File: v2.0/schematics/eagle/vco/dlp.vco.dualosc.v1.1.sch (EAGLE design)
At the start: 58 parts, among them IC1 NTE912P, IC2 TL074P, IC3 TL074P, J1 PWM IN1, J4 EXP.IN1, J6 OSC OUT1, Q1 2N3417, Q2 2N3417, Q3 2N3906

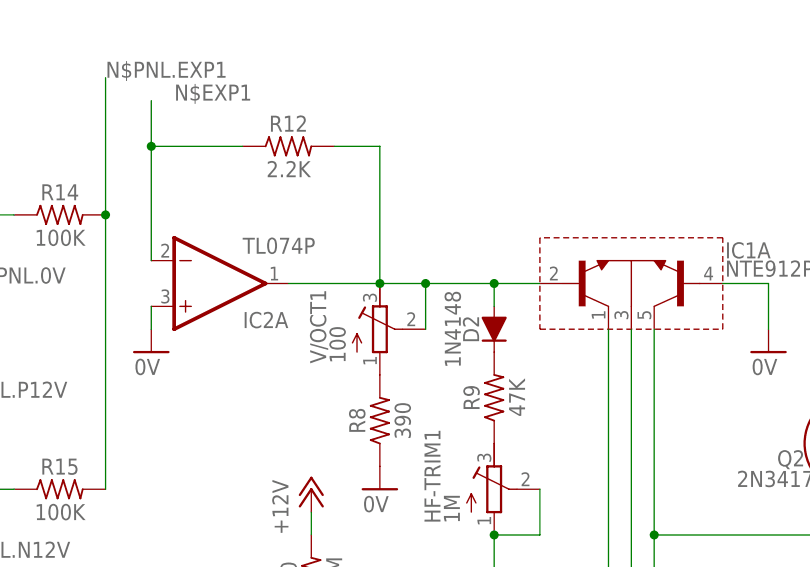
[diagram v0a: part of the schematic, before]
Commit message: Corrected errors on VCO across all versions (board needs to be regenerated)
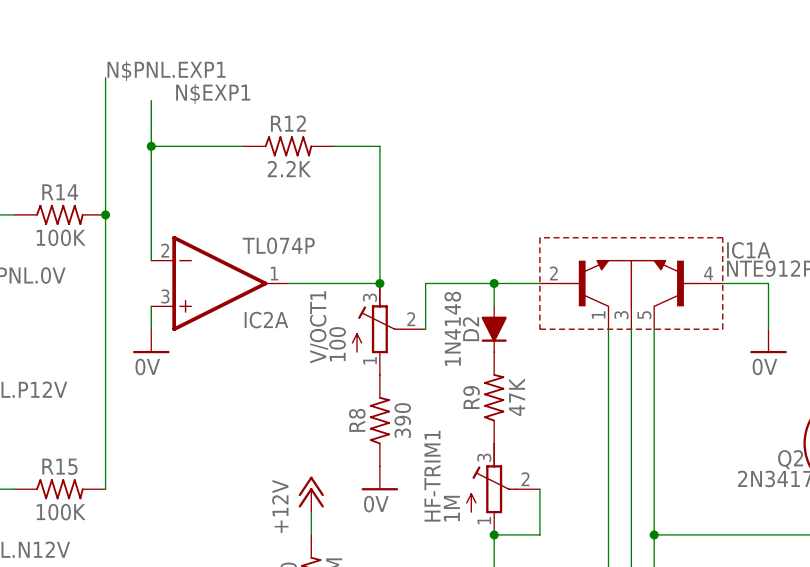
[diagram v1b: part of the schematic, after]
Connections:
- new net N$11: D2.A, IC1A.B1, V/OCT1.S
- net N$16: no longer D2.A, IC1A.B1, V/OCT1.S
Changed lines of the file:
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@@
 <pinref part="IC2" gate="A" pin="OUT"/>
 <wire x1="-17.78" y1="68.58" x2="-7.62" y2="68.58" width="0.1524" layer="91"/>
-<pinref part="D2" gate="G$1" pin="A"/>
-<pinref part="IC1" gate="A" pin="B1"/>
-<wire x1="10.16" y1="68.58" x2="5.08" y2="68.58" width="0.1524" layer="91"/>
-<wire x1="5.08" y1="68.58" x2="5.08" y2="66.04" width="0.1524" layer="91"/>
-<junction x="5.08" y="68.58"/>
-<wire x1="-2.54" y1="68.58" x2="5.08" y2="68.58" width="0.1524" layer="91"/>
-<wire x1="-2.54" y1="63.5" x2="-2.54" y2="68.58" width="0.1524" layer="91"/>
-<pinref part="V/OCT1" gate="G$1" pin="S"/>
-<wire x1="-7.62" y1="68.58" x2="-2.54" y2="68.58" width="0.1524" layer="91"/>
 <junction x="-7.62" y="68.58"/>
-<junction x="-2.54" y="68.58"/>
 </segment>
 </net>
@@
 </segment>
 </net>
+<net name="N$11" class="0">
+<segment>
+<pinref part="D2" gate="G$1" pin="A"/>
+<pinref part="IC1" gate="A" pin="B1"/>
+<wire x1="10.16" y1="68.58" x2="5.08" y2="68.58" width="0.1524" layer="91"/>
+<wire x1="5.08" y1="68.58" x2="5.08" y2="66.04" width="0.1524" layer="91"/>
+<junction x="5.08" y="68.58"/>
+<wire x1="-2.54" y1="68.58" x2="5.08" y2="68.58" width="0.1524" layer="91"/>
+<wire x1="-2.54" y1="63.5" x2="-2.54" y2="68.58" width="0.1524" layer="91"/>
+<pinref part="V/OCT1" gate="G$1" pin="S"/>
+</segment>
+</net>
